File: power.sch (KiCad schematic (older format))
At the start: 155 parts, among them J6 Conn_BAT, Q1 BSS138, Q2 BSS138, Q3 BSS138, Q4 BSS138, Q5 BSS138, SW1 SW_WAKEUP, SW2 SW_RESET, U1 SAMA5D2x-SIP, U2 ACT8945A

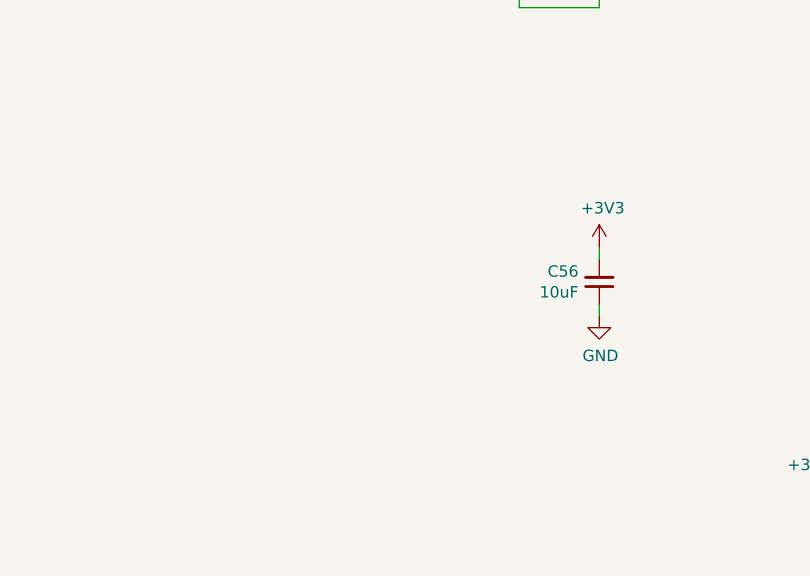
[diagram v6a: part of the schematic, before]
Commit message: Finish the routing, add bom, schematic
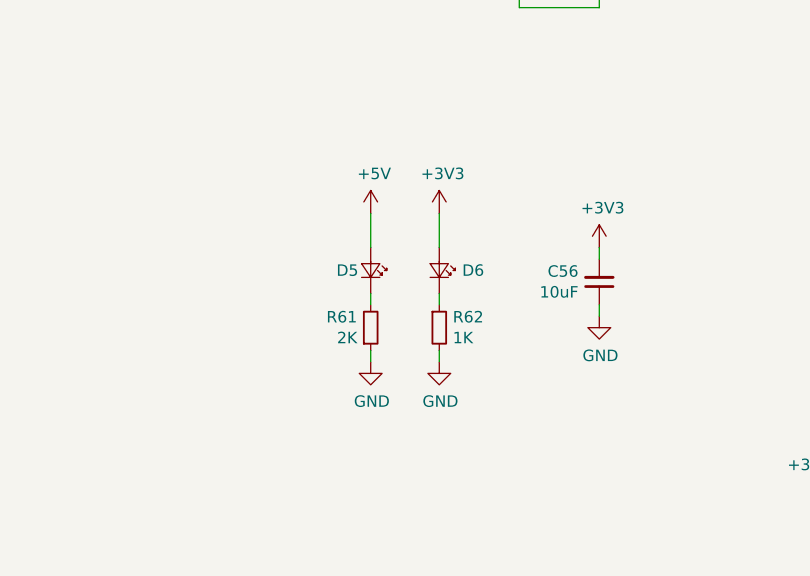
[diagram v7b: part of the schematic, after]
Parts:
- added D5: LED_5V, LED_SMD:LED_0603_1608Metric, symbol Device:LED_Small
- added D6: LED_3V, LED_SMD:LED_0603_1608Metric, symbol Device:LED_Small
- added R61: 2K, Resistor_SMD:R_0603_1608Metric, symbol Device:R_Small
- added R62: 1K, Resistor_SMD:R_0603_1608Metric, symbol Device:R_Small
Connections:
- net +3V3: now also D6.2 (A)
- net +5V: now also D5.2 (A)
- net GND: now also R61.1, R62.2
- new net: D5.1 (K), R61.2
- new net: D6.1 (K), R62.1
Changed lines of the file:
@@
 Wire Wire Line
 	11500 10750 11500 10900
+$Comp
+L power:+5V #PWR021
+U 1 1 5C7FB4C9
+P 10200 4600
+F 0 "#PWR021" H 10200 4450 50  0001 C CNN
+F 1 "+5V" H 10215 4773 50  0000 C CNN
+F 2 "" H 10200 4600 50  0001 C CNN
+F 3 "" H 10200 4600 50  0001 C CNN
+	1    10200 4600
+	1    0    0    -1
+$EndComp
+$Comp
+L power:+3V3 #PWR0166
+U 1 1 5C7FB723
+P 10500 4600
+F 0 "#PWR0166" H 10500 4450 50  0001 C CNN
+F 1 "+3V3" H 10515 4773 50  0000 C CNN
+F 2 "" H 10500 4600 50  0001 C CNN
+F 3 "" H 10500 4600 50  0001 C CNN
+	1    10500 4600
+	1    0    0    -1
+$EndComp
+Wire Wire Line
+	10200 4600 10200 4750
+$Comp
+L Device:LED_Small D5
+U 1 1 5C863E5C
+P 10200 4850
+F 0 "D5" V 10200 4700 50  0000 L CNN
+F 1 "LED_5V" V 10155 4948 50  0001 L CNN
+F 2 "LED_SMD:LED_0603_1608Metric" V 10200 4850 50  0001 C CNN
+F 3 "~" V 10200 4850 50  0001 C CNN
+	1    10200 4850
+	0    1    -1   0
+$EndComp
+Wire Wire Line
+	10200 4950 10200 5000
+$Comp
+L Device:R_Small R61
+U 1 1 5CA6D0A0
+P 10200 5100
+F 0 "R61" H 10141 5054 50  0000 R CNN
+F 1 "2K" H 10141 5145 50  0000 R CNN
+F 2 "Resistor_SMD:R_0603_1608Metric" H 10200 5100 50  0001 C CNN
+F 3 "~" H 10200 5100 50  0001 C CNN
+	1    10200 5100
+	1    0    0    1
+$EndComp
+Wire Wire Line
+	10200 5200 10200 5250
+$Comp
+L power:GND #PWR022
+U 1 1 5CAD5BDD
+P 10200 5250
+F 0 "#PWR022" H 10200 5000 50  0001 C CNN
+F 1 "GND" H 10205 5077 50  0000 C CNN
+F 2 "" H 10200 5250 50  0001 C CNN
+F 3 "" H 10200 5250 50  0001 C CNN
+	1    10200 5250
+	1    0    0    -1
+$EndComp
+Wire Wire Line
+	10500 4600 10500 4750
+$Comp
+L Device:LED_Small D6
+U 1 1 5CF52B83
+P 10500 4850
+F 0 "D6" V 10500 4950 50  0000 L CNN
+F 1 "LED_3V" V 10455 4948 50  0001 L CNN
+F 2 "LED_SMD:LED_0603_1608Metric" V 10500 4850 50  0001 C CNN
+F 3 "~" V 10500 4850 50  0001 C CNN
+	1    10500 4850
+	0    1    -1   0
+$EndComp
+Wire Wire Line
+	10500 4950 10500 5000
+$Comp
+L Device:R_Small R62
+U 1 1 5CF52B8E
+P 10500 5100
+F 0 "R62" H 10559 5146 50  0000 L CNN
+F 1 "1K" H 10559 5055 50  0000 L CNN
+F 2 "Resistor_SMD:R_0603_1608Metric" H 10500 5100 50  0001 C CNN
+F 3 "~" H 10500 5100 50  0001 C CNN
+	1    10500 5100
+	1    0    0    -1
+$EndComp
+Wire Wire Line
+	10500 5200 10500 5250
+$Comp
+L power:GND #PWR0193
+U 1 1 5CF52B99
+P 10500 5250
+F 0 "#PWR0193" H 10500 5000 50  0001 C CNN
+F 1 "GND" H 10505 5077 50  0000 C CNN
+F 2 "" H 10500 5250 50  0001 C CNN
+F 3 "" H 10500 5250 50  0001 C CNN
+	1    10500 5250
+	1    0    0    -1
+$EndComp
 $EndSCHEMATC
